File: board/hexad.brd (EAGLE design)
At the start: 160 x 100 mm, 0 parts

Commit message: added more parts
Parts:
- added C1, C3: 47uF@50V, holla:C-E-6
- added C10, C11, C2, C4: 1u, holla:C-0603
- added C5, C7, C8, C9: .1u, holla:C-0603
- added C6: DNP, holla:C-0603
- added D3: VZ10, holla:D-SOD323
- added D4: GRN, holla:LED-0603
- added J1, JCYCLE, JDOOR, JFEED: (no value), holla:CONN-3.81MM-KF2EDG-2
- added J11: (no value), holla:CONN-MICROSD-2908-05WB-MG
- added J2: (no value), holla:CONN-.100-4
- added J3: (no value), holla:1X08
- added JA, JSPINDLE, JX, JY, JZ: (no value), holla:CONN-3.81MM-KF2EDG-6
- added JP1, JP2: FIDUCIAL-MICRO, holla:FIDUCIAL-MICRO
- added Q1: 40V, holla:SOT23-3
- added Q10, Q11, Q12, Q13, Q2, Q3, Q4, Q5, Q6, Q7, Q8, Q9: (no value), holla:SOT23-3
- added R1: 100k, holla:R-0603
- added R10, R12, R16, R20, R22, R4, R7: 10k, holla:R-0603
- added R11, R15, R19, R21, R5, R8, R9: 100, holla:R-0603
- added R13, R14: 2k, holla:R-0603
- added R17, R18: DNP, holla:R-0603
- added R2, R3: (no value), holla:R-0603
- added R23, R6: 1k, holla:R-0603
- added S1: (no value), holla:SWITCH-EVQ5PN
- added TP1, TP2, TP3, TPG: (no value), holla:TPTHRU
- added U1: RADIO-ESP32_DEVKIT, holla:ESP32_DEVKIT
- added U2: R-78E5.0-1.0, holla:VREG-SIP3
- added U3: (no value), holla:SO28W
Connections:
- new net 24V0: C1.+, D3.C, JA.6, JSPINDLE.6, JX.6, JY.6, JZ.6, Q1.2, U2.1
- new net 3V3: C10.2, C2.2, C4.2, J11.4, Q2.1, R10.2, R12.2, R13.2, R14.2, R16.2, R18.2, R20.2, R22.2, R23.2, R3.2, R4.2, R7.2, U1.3V3, U3.9
- new net 5V0: C3.+, JA.5, JSPINDLE.5, JX.5, JY.5, JZ.5, R2.2, R6.2, U1.VIN, U2.3
- new net A_DIR: Q10.1, U1.D2
- new net A_LIMIT: C9.1, R11.2, U1.D4
- new net A_STEP: Q9.1, U1.D15
- new net CS_SD: J11.2, U1.D34
- new net CYCLE_START: R21.2, U1.VN
- new net DOOR: R15.2
- new net FEED_HOLD: R19.2, U1.VP
- new net GND: C1.-, C10.1, C11.1, C2.1, C3.-, C4.1, C5.2, C6.2, C7.2, C8.2, C9.2, D4.C, J1.1, J11.6, J11.MT1, J11.MT2, J3.1, JA.1, JCYCLE.1, JDOOR.1, JFEED.1, JSPINDLE.1, JX.1, JY.1, JZ.1, Q10.2, Q11.2, Q12.2, Q13.2, Q3.2, Q4.2, Q5.2, Q6.2, Q7.2, Q8.2, Q9.2, R1.1, S1.1, TPG.1, U1.GND@1, U1.GND@2, U2.2, U3.10, U3.15, U3.16, U3.17
- new net MISO: J11.7, TP2.1, U1.D19
- new net MOSI: J11.3, TP1.1, U1.D23
- new net N$1: J1.2, Q1.3
- new net N$10: JA.4, R11.1, R12.1
- new net N$11: JA.2, Q10.3
- new net N$12: JDOOR.2, R15.1, R16.1
- new net N$13: JSPINDLE.4, Q13.3, R17.1, R18.1
- new net N$14: JSPINDLE.2, Q12.3
- new net N$15: J3.5
- new net N$16: JFEED.2, R19.1, R20.1
- new net N$17: JCYCLE.2, R21.1, R22.1
- new net N$18: J2.4
- new net N$19: J2.3
- new net N$2: JX.4, R4.1, R8.1
- new net N$20: J2.2
- new net N$21: J2.1
- new net N$22: J3.4
- new net N$23: J3.3
- new net N$24: D3.A, Q1.1, R1.2
- new net N$25: J3.2
- new net N$26: J3.7
- new net N$3: Q2.2, R3.1
- new net N$4: Q2.3, R2.1
- new net N$5: JX.2, Q4.3
- new net N$6: JY.4, R5.1, R7.1
- new net N$7: JY.2, Q6.3
- new net N$8: JZ.4, R10.1, R9.1
- new net N$84: D4.A, R6.1
- new net N$9: JZ.2, Q8.3
- new net RESET: C11.2, R23.1, S1.2, U1.EN, U3.18
- new net SCK: J11.5, TP3.1, U1.D18
- new net SCL: R14.1, U1.D22, U3.12
- new net SDA: R13.1, U1.D21, U3.13
- new net SPINDLE_DIR: Q12.1, U1.TX2
- new net SPINDLE_ENABLE: C6.1, Q13.1, R17.2, U1.D5
- new net SPINDLE_PWM: Q11.1, U1.RX2
- new net X_DIR: Q4.1, U1.D12
- new net X_LIMIT: C5.1, R8.2, U1.D14
- new net X_STEP: Q3.1, U1.D13
- new net X_STEP_5V0: JX.3, Q3.3
- new net X_STEP_5V1: JY.3, Q5.3
- new net X_STEP_5V2: JZ.3, Q7.3
- new net X_STEP_5V3: JA.3, Q9.3
- new net X_STEP_5V4: JSPINDLE.3, Q11.3
- new net Y_DIR: Q6.1, U1.D26
- new net Y_LIMIT: C7.1, R5.2, U1.D25
- new net Y_STEP: Q5.1, U1.D27
- new net Z_DIR: Q8.1, U1.D32
- new net Z_LIMIT: C8.1, R9.2, U1.D35
- new net Z_STEP: Q7.1, U1.D33
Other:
- board size 160 x 100 mm -> 100 x 100 mm

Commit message: started routing
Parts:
- removed J1, JCYCLE, JDOOR, JFEED: (no value), holla:CONN-3.81MM-KF2EDG-2
- removed J2: (no value), holla:CONN-.100-4
- removed J3: (no value), holla:1X08
- removed JA, JSPINDLE, JY, JZ: (no value), holla:CONN-3.81MM-KF2EDG-6
- removed S1: (no value), holla:SWITCH-EVQ5PN
- removed TP1, TP2, TP3: (no value), holla:TPTHRU
- added 24V0, 3V3, 5V0, MISO, MOSI, SCK: (no value), holla:TPTHRU
- added A, SPINDLE, Y, Z: (no value), holla:CONN-3.81MM-KF2EDG-6
- added C12, C13, C14, C15: .1u, holla:C-0603
- added CYCLE, FEED, VIN: (no value), holla:CONN-3.81MM-KF2EDG-2
- added DISPLAY: (no value), holla:1X08
- added I2C: (no value), holla:CONN-.100-4
- added J24V0, J3V3, J5V0, LED0, LED1, LED2, LED3, RESET, USER0, USER1, USER2, USER3: (no value), holla:CONN-.100-2
- added R24, R25: 220, holla:R-0603
- added R26, R27: 100, holla:R-0603
- Q1: device holla:SOT23-3 -> holla:TO252
- R15: value 100 -> 220
- R16: value 10k -> 220
- moved C11 758.3 mm to (45.0, 91.0), turned to 180 degrees
- moved R23 750.4 mm to (45.0, 88.0)
- moved C10 739.8 mm to (15.0, 85.0), turned to 90 degrees
- moved U3 724.0 mm to (25.0, 80.0)
- moved C8 676.9 mm to (45.0, 83.0)
- moved C9 667.9 mm to (60.0, 68.0), turned to 180 degrees
- moved C7 665.3 mm to (45.0, 75.4)
- moved C6 663.5 mm to (60.0, 75.4), turned to 180 degrees
- moved C5 650.1 mm to (45.0, 68.0)
- moved R21 616.1 mm to (13.0, 42.0), turned to 90 degrees
- moved R22 611.1 mm to (13.0, 37.3), turned to 270 degrees
- moved R19 601.2 mm to (13.0, 53.0), turned to 90 degrees
- moved R20 596.6 mm to (13.0, 48.8), turned to 270 degrees
- moved Q13 584.5 mm to (87.0, 57.0), turned to 180 degrees
- moved R18 579.7 mm to (87.0, 63.0)
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- renumbered JX to X
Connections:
- removed net DOOR: R15.2
- removed net N$21: J2.1
- new net DISPLAY_CS: DISPLAY.7, U3.25
- new net DISPLAY_DC: DISPLAY.6, U3.26
- new net N$27: LED2.2, R24.2
- new net N$28: LED1.2, R16.2
- new net N$29: LED0.2, R15.2
- new net USER0: C12.1, U3.1, USER0.2
- new net USER1: C13.1, U3.2, USER1.2
- new net USER2: C14.1, U3.3, USER2.2
- new net USER3: C15.1, U3.4, USER3.2
- net 24V0: now also 24V0.1, A.6, J24V0.2, SPINDLE.6, Y.6, Z.6; no longer JA.6, JSPINDLE.6, JY.6, JZ.6
- net 3V3: now also 3V3.1, J3V3.2; no longer R16.2
- net 5V0: now also 5V0.1, A.5, I2C.2, J5V0.2, SPINDLE.5, Y.5, Z.5; no longer JA.5, JSPINDLE.5, JY.5, JZ.5
- net GND: now also A.1, C12.2, C13.2, C14.2, C15.2, CYCLE.1, DISPLAY.1, FEED.1, I2C.1, J24V0.1, J3V3.1, J5V0.1, LED0.1, LED1.1, LED2.1, LED3.1, RESET.1, SPINDLE.1, USER0.1, USER1.1, USER2.1, USER3.1, VIN.1, Y.1, Z.1; no longer J1.1, J3.1, JA.1, JCYCLE.1, JDOOR.1, JFEED.1, JSPINDLE.1, JY.1, JZ.1, S1.1
- net MISO: now also MISO.1; no longer TP2.1
- net MOSI: now also DISPLAY.4, MOSI.1; no longer TP1.1
- net N$1: now also VIN.2; no longer J1.2
- net N$10: now also A.4; no longer JA.4
- net N$11: now also A.2; no longer JA.2
- net N$12: now also U3.21; no longer JDOOR.2, R16.1
- net N$13: now also SPINDLE.4; no longer JSPINDLE.4
- net N$14: now also SPINDLE.2; no longer JSPINDLE.2
- net N$15: now also R16.1, U3.22; no longer J3.5
- net N$16: now also FEED.2; no longer JFEED.2
- net N$17: now also CYCLE.2; no longer JCYCLE.2
- net N$18: now also I2C.4, R27.1; no longer J2.4
- net N$19: now also I2C.3, R26.1; no longer J2.3
- net N$20: now also DISPLAY.8; no longer J2.2
- net N$22: now also R24.1, U3.23; no longer J3.4
- net N$23: now also R25.1, U3.24; no longer J3.3
- net N$25: now also DISPLAY.2; no longer J3.2
- net N$26: now also LED3.2, R25.2; no longer J3.7
- net N$6: now also Y.4; no longer JY.4
- net N$7: now also Y.2; no longer JY.2
- net N$8: now also Z.4; no longer JZ.4
- net N$9: now also Z.2; no longer JZ.2
- net RESET: now also DISPLAY.5, RESET.2; no longer S1.2
- net SCK: now also DISPLAY.3, SCK.1; no longer TP3.1
- net SCL: now also R27.2
- net SDA: now also R26.2
- net X_STEP_5V1: now also Y.3; no longer JY.3
- net X_STEP_5V2: now also Z.3; no longer JZ.3
- net X_STEP_5V3: now also A.3; no longer JA.3
- net X_STEP_5V4: now also SPINDLE.3; no longer JSPINDLE.3
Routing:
- net 24V0: track 0.00 -> 208.8 mm
- net 5V0: track 0.00 -> 159.6 mm
- net Z_LIMIT: track 0.00 -> 101.3 mm
- net Z_STEP: track 0.00 -> 98.6 mm
- net Z_DIR: track 0.00 -> 94.1 mm, vias 0 -> 1
- net Y_LIMIT: track 0.00 -> 73.6 mm
- net X_LIMIT: track 0.00 -> 71.9 mm, vias 0 -> 2
- net X_DIR: track 0.00 -> 71.0 mm, vias 0 -> 2
- net CYCLE_START: track 0.00 -> 70.0 mm, vias 0 -> 1
- net Y_STEP: track 0.00 -> 69.4 mm
- net X_STEP: track 0.00 -> 68.0 mm, vias 0 -> 2
- net A_DIR: track 0.00 -> 67.8 mm
- net Y_DIR: track 0.00 -> 66.8 mm, vias 0 -> 1
- net SCL: track 0.00 -> 62.7 mm
- net FEED_HOLD: track 0.00 -> 62.6 mm, vias 0 -> 1
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
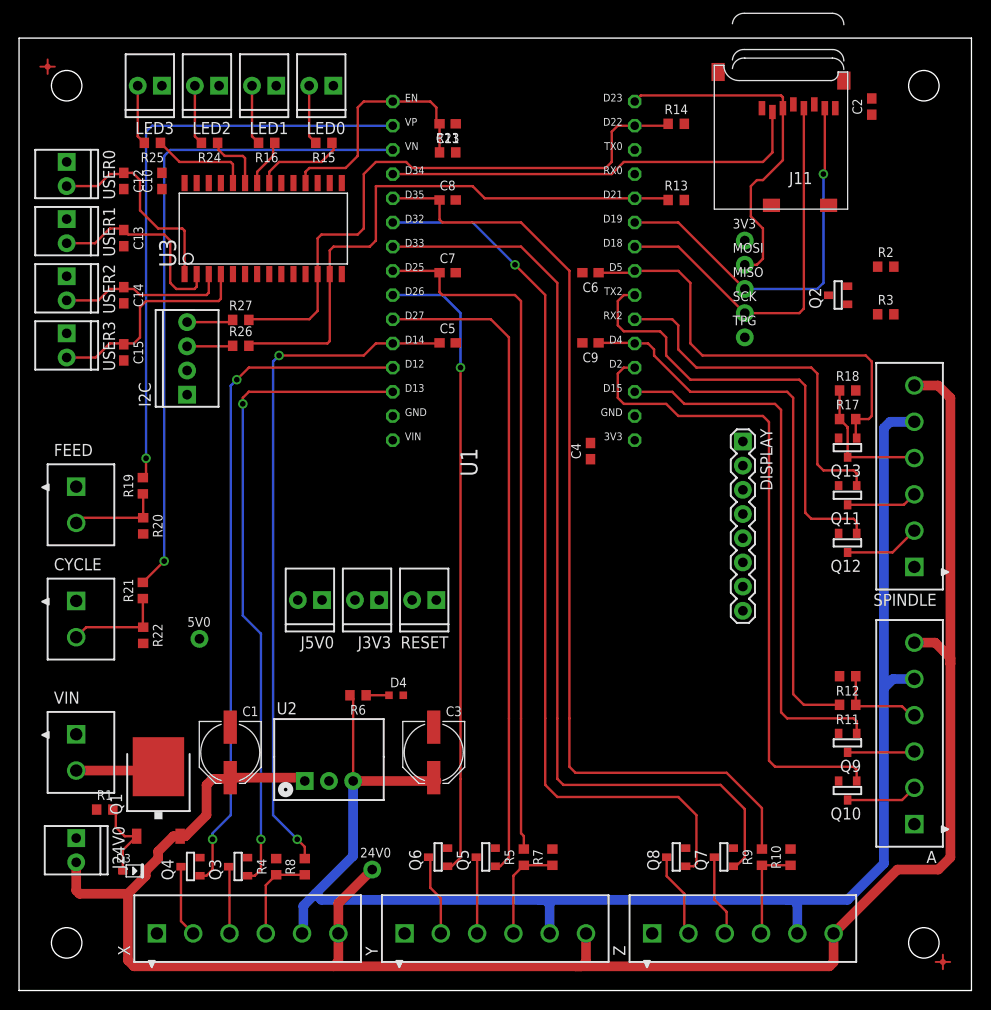
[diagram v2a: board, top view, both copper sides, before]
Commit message: changed connectors to 0.1 headers
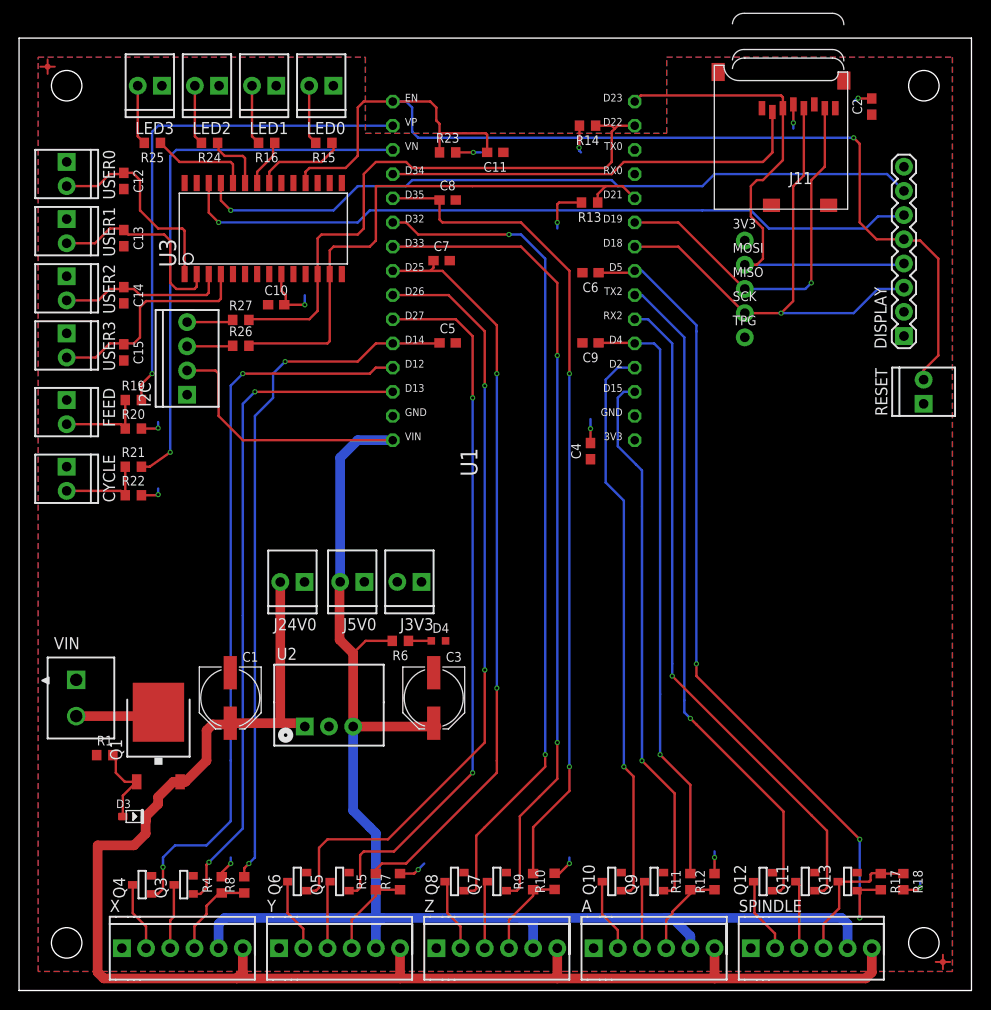
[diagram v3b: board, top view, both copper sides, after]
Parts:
- removed 24V0, 5V0: (no value), holla:TPTHRU
- removed Q2: (no value), holla:SOT23-3
- removed R2, R3: (no value), holla:R-0603
- A, SPINDLE, X, Y, Z: device holla:CONN-3.81MM-KF2EDG-6 -> holla:CONN-.100-6
- CYCLE, FEED: device holla:CONN-3.81MM-KF2EDG-2 -> holla:CONN-.100-2
- moved RESET 55.2 mm to (95.0, 61.6), turned to 90 degrees
- moved SPINDLE 52.4 mm to (76.8, 4.45), turned to 0 degrees
- moved R18 51.9 mm to (92.8, 11.4), turned to 270 degrees
- moved R17 48.7 mm to (90.5, 11.4), turned to 270 degrees
- moved Q13 45.6 mm to (87.0, 11.4), turned to 90 degrees
- moved Q11 40.8 mm to (82.5, 11.4), turned to 90 degrees
- moved A 40.5 mm to (60.3, 4.45), turned to 0 degrees
- moved Q12 36.7 mm to (78.1, 11.4), turned to 90 degrees
- moved J24V0 36.0 mm to (30.0, 42.9), turned to 180 degrees
- moved Z 32.2 mm to (43.8, 4.45)
- moved Q10 26.6 mm to (62.2, 11.4), turned to 90 degrees
- moved R12 25.7 mm to (73.0, 11.4), turned to 90 degrees
- moved Q9 25.0 mm to (66.7, 11.4), turned to 90 degrees
- moved R10 24.9 mm to (56.2, 11.5)
- moved R11 24.9 mm to (70.5, 11.4), turned to 90 degrees
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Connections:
- removed net N$3: Q2.2, R3.1
- removed net N$4: Q2.3, R2.1
- net 24V0: no longer 24V0.1
- net 3V3: no longer Q2.1, R3.2
- net 5V0: no longer 5V0.1, R2.2
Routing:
- net RESET: track 26.1 -> 116.7 mm, vias 0 -> 1
- net DISPLAY_DC: track 0.00 -> 78.4 mm, vias 0 -> 1
- net DISPLAY_CS: track 0.00 -> 76.8 mm, vias 0 -> 1
- net 24V0: track 208.8 -> 156.6 mm
- net 3V3: track 0.00 -> 42.0 mm, vias 0 -> 14
- net SPINDLE_ENABLE: track 46.0 -> 87.5 mm, vias 0 -> 3
- net SPINDLE_PWM: track 38.4 -> 70.3 mm, vias 0 -> 1
- net SPINDLE_DIR: track 48.3 -> 70.4 mm, vias 0 -> 1
- net 5V0: track 159.6 -> 181.5 mm
- net MOSI: track 37.3 -> 54.1 mm
- net Y_DIR: track 66.8 -> 82.0 mm, vias 1 -> 2
- net Z_LIMIT: track 101.3 -> 87.8 mm, vias 0 -> 2
- net Z_STEP: track 98.6 -> 85.5 mm, vias 0 -> 2
- net SCK: track 41.9 -> 54.8 mm, vias 0 -> 1
- net CYCLE_START: track 70.0 -> 58.2 mm
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- added copper zone on layer 16, net 3V3
- added copper zone on layer 1, net GND
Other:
- board text added: "hexad 191101 v1.0"

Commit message: release v1.0
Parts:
- removed Q13: (no value), holla:SOT23-3
- added Q2: (no value), holla:SOT23-3
- added R2, R3: 220, holla:R-0603
- C1: value 47uF@50V -> 1u; device holla:C-E-6 -> holla:C-0603
- C10, C11, C4: value 1u -> .1u
- C13, C9: value .1u -> 1u
- C14, C15: value .1u -> 47uF@50V; device holla:C-0603 -> holla:C-E-6
- C3: value 47uF@50V -> .1u; device holla:C-E-6 -> holla:C-0603
- C6: value DNP -> .1u
- C7: value .1u -> DNP
- R1: value 100k -> 2k
- R10, R12, R22: value 10k -> 100
- R13: value 2k -> 10k
- R14: value 2k -> 100
- R15: value 220 -> 10k
- R16: value 220 -> 1k
- R17: value DNP -> 100k
- R18: value DNP -> 10k
- R23: value 1k -> 10k
- R24, R25: value 220 -> DNP
- R26: value 100 -> 10k
- R4: value 10k -> 220
- R5: value 100 -> 220
- R7: value 10k -> 2k
- U1: value RADIO-ESP32_DEVKIT -> (none); device holla:ESP32_DEVKIT -> holla:SO28W
- U2: value R-78E5.0-1.0 -> RADIO-ESP32_DEVKIT; device holla:VREG-SIP3 -> holla:ESP32_DEVKIT
- U3: value (none) -> R-78E5.0-1.0; device holla:SO28W -> holla:VREG-SIP3
- moved R25 110.6 mm to (92.8, 11.4), turned to 270 degrees
- moved R24 104.8 mm to (90.5, 11.4), turned to 270 degrees
- moved R8 91.7 mm to (88.3, 76.2), turned to 180 degrees
- moved C1 91.6 mm to (89.5, 92.8), turned to 90 degrees
- moved R1 83.3 mm to (59.7, 90.8), turned to 180 degrees
- moved R17 82.6 mm to (9.00, 24.7), turned to 0 degrees
- moved R23 81.5 mm to (73.0, 11.4), turned to 90 degrees
- moved R12 79.3 mm to (12.0, 62.0), turned to 0 degrees
- moved R4 78.0 mm to (26.0, 89.0), turned to 180 degrees
- moved R5 77.8 mm to (32.0, 89.0), turned to 180 degrees
- moved R7 74.0 mm to (59.9, 82.7), turned to 180 degrees
- moved R11 73.4 mm to (23.3, 67.7), turned to 0 degrees
- moved R22 71.2 mm to (70.5, 11.4), turned to 90 degrees
- moved R9 71.1 mm to (88.3, 73.7), turned to 180 degrees
- moved Q11 69.6 mm to (12.9, 11.1)
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- renumbered D3 to D2, D4 to D1, J11 to J1, JP1 to FID1, JP2 to FID2, TPG to GND
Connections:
- removed net N$25: DISPLAY.2
- new net N$3: DISPLAY.3, R9.1
- new net N$4: DISPLAY.4, R8.1
- net 24V0: now also C14.+, U3.1; no longer C1.+, U2.1
- net 3V3: now also C1.2, C13.2, C9.2, R1.2, R15.2, R25.2, R26.2, R6.2, U1.9, U2.3V3; no longer C10.2, C2.2, C4.2, R10.2, R12.2, R14.2, R22.2, R4.2, U1.3V3, U3.9
- net 5V0: now also C15.+, DISPLAY.2, R16.2, U2.VIN, U3.3; no longer C3.+, R6.2, U1.VIN, U2.3
- net A_DIR: now also Q6.1, U2.D2; no longer Q10.1, U1.D2
- net A_LIMIT: now also C11.1, R22.2, U2.D4; no longer C9.1, R11.2, U1.D4
- net A_STEP: now also Q7.1, U2.D15; no longer Q9.1, U1.D15
- net CS_SD: now also U2.D34; no longer U1.D34
- net CYCLE_START: now also R14.2, U2.VN; no longer R21.2, U1.VN
- net DISPLAY_CS: now also U1.25; no longer U3.25
- net DISPLAY_DC: now also U1.26; no longer U3.26
- net FEED_HOLD: now also R12.2, U2.VP; no longer R19.2, U1.VP
- net GND: now also C1.1, C10.2, C11.2, C13.1, C14.-, C15.-, C3.2, C4.2, C9.1, Q2.2, R17.1, U1.10, U1.15, U1.16, U1.17, U2.GND@1, U2.GND@2, U3.2; no longer C1.-, C10.1, C11.1, C13.2, C14.2, C15.2, C3.-, C4.1, C9.2, Q13.2, R1.1, U1.GND@1, U1.GND@2, U2.2, U3.10, U3.15, U3.16, U3.17
- net MISO: now also U2.D19; no longer U1.D19
- net MOSI: now also R8.2, U2.D23; no longer DISPLAY.4, U1.D23
- net N$10: now also R22.1, R23.1; no longer R11.1, R12.1
- net N$11: now also Q6.3; no longer Q10.3
- net N$12: now also R5.1, U1.21; no longer R15.1, U3.21
- net N$13: now also Q9.3, R24.1, R25.1; no longer Q13.3, R17.1, R18.1
- net N$14: now also Q10.3; no longer Q12.3
- net N$15: now also R4.1, U1.22; no longer R16.1, U3.22
- net N$16: now also R12.1, R13.1; no longer R19.1, R20.1
- net N$17: now also R14.1, R15.1; no longer R21.1, R22.1
- net N$18: now also R10.1; no longer R27.1
- net N$19: now also R11.1; no longer R26.1
- net N$2: now also R26.1, R27.1; no longer R4.1, R8.1
- net N$22: now also R3.1, U1.23; no longer R24.1, U3.23
- net N$23: now also R2.1, U1.24; no longer R25.1, U3.24
- net N$24: now also R17.2; no longer R1.2
- net N$26: now also R2.2; no longer R25.2
- net N$27: now also R3.2; no longer R24.2
- net N$28: now also R4.2; no longer R16.2
- net N$29: now also R5.2; no longer R15.2
- net N$5: now also Q11.3; no longer Q4.3
- net N$6: now also R19.1, R20.1; no longer R5.1, R7.1
- net N$7: now also Q2.3; no longer Q6.3
- net N$8: now also R18.1, R21.1; no longer R10.1, R9.1
- net N$84: now also R16.1; no longer R6.1
- net N$9: now also Q4.3; no longer Q8.3
- net RESET: now also C2.2, R6.1, U1.18, U2.EN; no longer C11.2, R23.1, U1.EN, U3.18
- net SCK: now also R9.2, U2.D18; no longer DISPLAY.3, U1.D18
- net SCL: now also R1.1, R10.2, U1.12, U2.D22; no longer R14.1, R27.2, U1.D22, U3.12
- net SDA: now also R11.2, R7.1, U1.13, U2.D21; no longer R13.1, R26.2, U1.D21, U3.13
- net SPINDLE_DIR: now also Q10.1, U2.RX2; no longer Q12.1, U1.TX2
- net SPINDLE_ENABLE: now also C7.1, Q9.1, R24.2, U2.D5; no longer C6.1, Q13.1, R17.2, U1.D5
- net SPINDLE_PWM: now also Q8.1, U2.TX2; no longer Q11.1, U1.RX2
- net USER0: now also C3.1, U1.1; no longer C12.1, U3.1
- net USER1: now also C5.1, U1.2; no longer C13.1, U3.2
- net USER2: now also C8.1, U1.3; no longer C14.1, U3.3
- net USER3: now also C12.1, U1.4; no longer C15.1, U3.4
- net X_DIR: now also Q11.1, U2.D12; no longer Q4.1, U1.D12
- net X_LIMIT: now also C10.1, R27.2, U2.D14; no longer C5.1, R8.2, U1.D14
- net X_STEP: now also Q12.1, U2.D13; no longer Q3.1, U1.D13
- net X_STEP_5V0: now also Q12.3; no longer Q3.3
- net X_STEP_5V1: now also Q3.3; no longer Q5.3
- net X_STEP_5V2: now also Q5.3; no longer Q7.3
- net X_STEP_5V3: now also Q7.3; no longer Q9.3
- net X_STEP_5V4: now also Q8.3; no longer Q11.3
- net Y_DIR: now also Q2.1, U2.D26; no longer Q6.1, U1.D26
- net Y_LIMIT: now also C6.1, R19.2, U2.D25; no longer C7.1, R5.2, U1.D25
- net Y_STEP: now also Q3.1, U2.D27; no longer Q5.1, U1.D27
- net Z_DIR: now also Q4.1, U2.D32; no longer Q8.1, U1.D32
- net Z_LIMIT: now also C4.1, R21.2, U2.D35; no longer C8.1, R9.2, U1.D35
- net Z_STEP: now also Q5.1, U2.D33; no longer Q7.1, U1.D33
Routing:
- net 5V0: track 181.5 -> 248.6 mm, vias 0 -> 2
- net MOSI: track 54.1 -> 48.5 mm, vias 0 -> 1
- net SCK: track 54.8 -> 50.1 mm, vias 1 -> 2
- net N$3: track 0.00 -> 3.85 mm
- net N$4: track 0.00 -> 3.85 mm
- net SPINDLE_PWM: track 70.3 -> 72.8 mm
- net SPINDLE_DIR: track 70.4 -> 68.3 mm
